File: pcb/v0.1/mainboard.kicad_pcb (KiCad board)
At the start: 2 copper layers, 123 parts, among them J1 Conn_01x02_Pin, J10 Conn_01x02_Pin, J11 Conn_01x02_Pin, J12 Conn_02x08_Odd_Even, J13 Conn_02x08_Odd_Even, J2 TYPE_C_Receptacle, J3 Conn_01x04_Pin, J4 TYPE_C_Receptacle, J5 TYPE_C_Receptacle, J6 22s_disp_connector, J7 ComputeModule5-CM5_connector, J8 Micro_SD_molex, J9 AudioJack3, Q1 MMBT2222A, SW1 SW_Push_45deg, U1 AP2112K-3.3TRG1, U2 Nexperia PUSB3FR4Z, U3 Nexperia PUSB3FR4Z, U4 PCM5102A, U5 RT9742GGJ5, U6 RT9742GGJ5, U7 MDBT50Q-P1MV2, U8 AP22653W6-7, Y1 O_32.768kHz

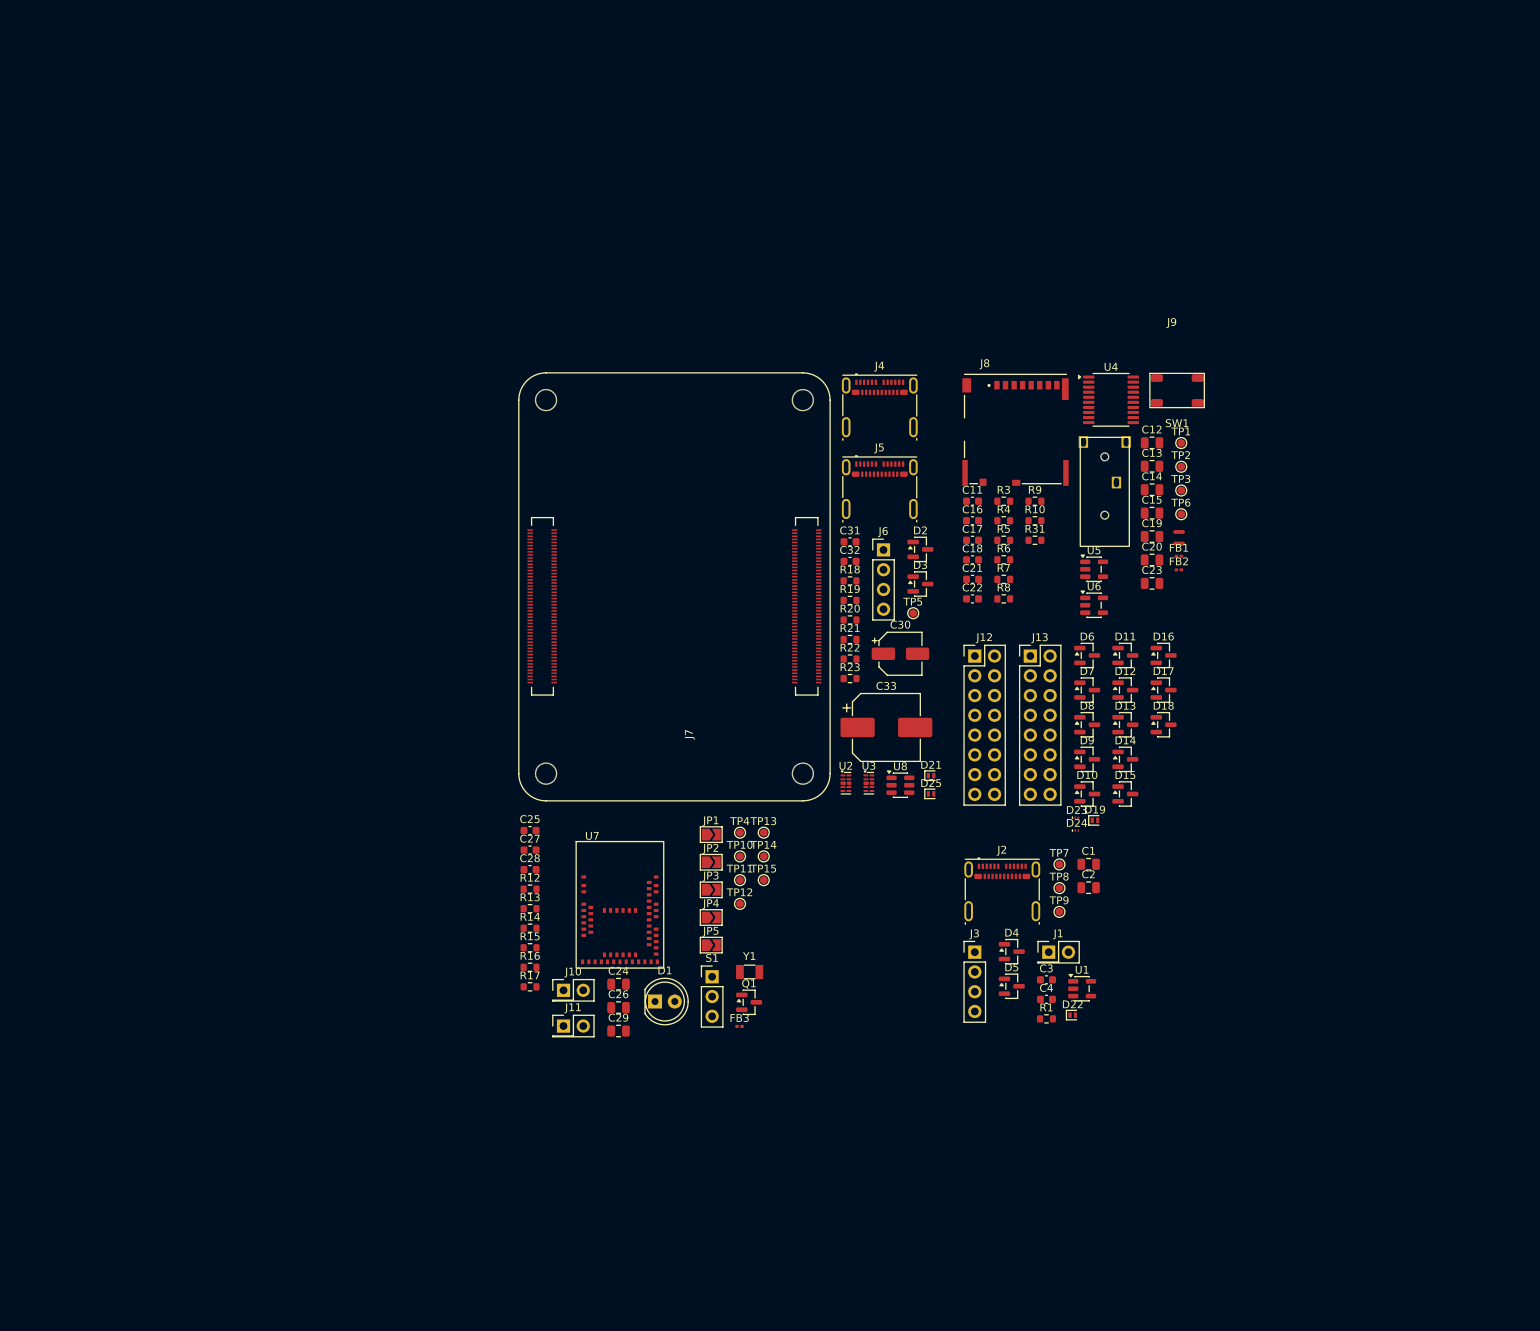
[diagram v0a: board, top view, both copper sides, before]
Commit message: Board setup and basic layout grouping
* Added board setup settings according to JLCpcbs manufacturing minimums
  (and generous extra)
* Grouped related components on the pcb
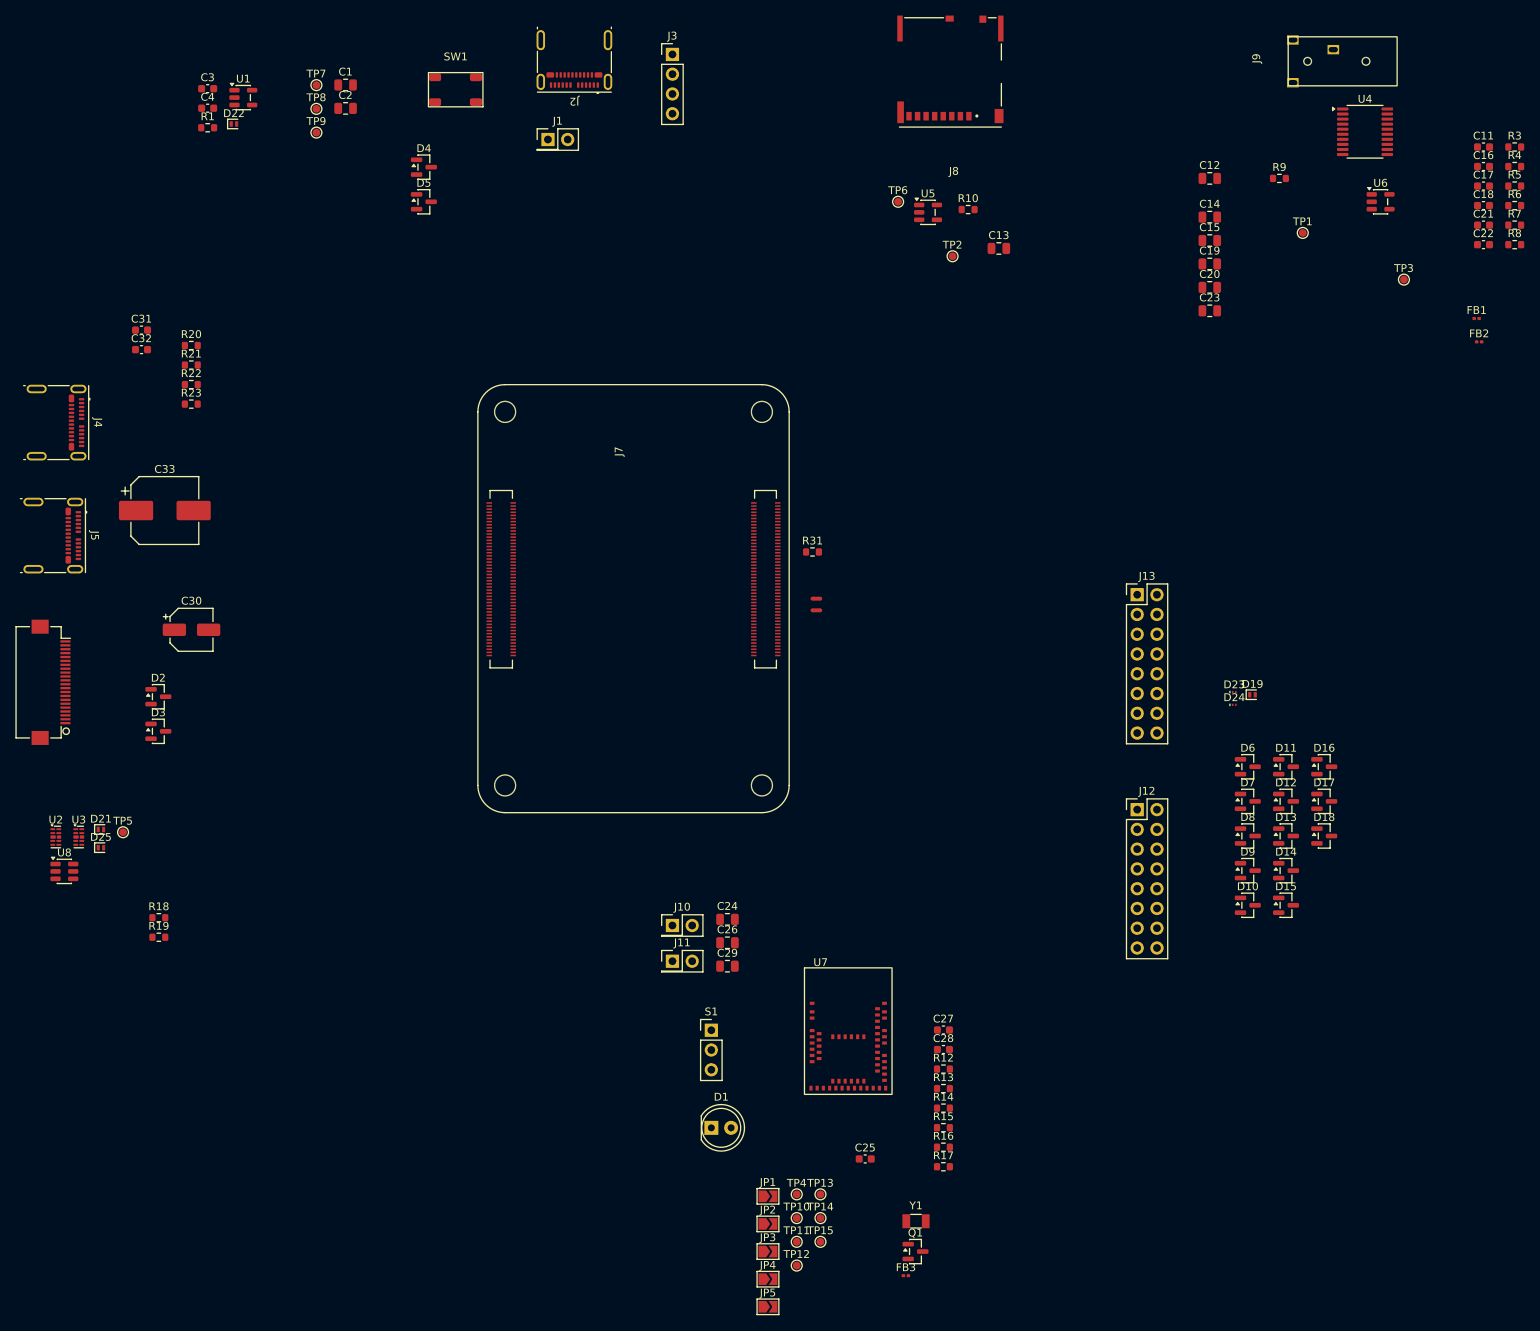
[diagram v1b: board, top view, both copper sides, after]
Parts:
- J6: footprint Connector_PinHeader_2.54mm:PinHeader_1x04_P2.54mm_Vertical -> CM5IO:Hirose_FH12-22S-0.5SH_1x22-1MP_P0.50mm_Horizontal
- moved R1 157.3 mm to (50.3, 54.5)
- moved U1 157.3 mm to (54.9, 50.6)
- moved C3 157.3 mm to (50.3, 49.5)
- moved C4 157.3 mm to (50.3, 52.0)
- moved D22 157.3 mm to (53.6, 54.0)
- moved C1 138.4 mm to (68.0, 49.0)
- moved C2 138.4 mm to (68.0, 52.0)
- moved TP7 138.4 mm to (64.2, 49.0)
- moved TP8 138.4 mm to (64.2, 52.1)
- moved TP9 138.4 mm to (64.2, 55.1)
- moved D5 126.0 mm to (78.1, 64.0)
- moved D4 126.0 mm to (78.1, 59.5)
- moved J1 122.7 mm to (94.0, 56.0)
- moved J3 121.7 mm to (110.0, 45.1)
- moved J2 120.1 mm to (97.4, 45.8), turned to 180 degrees
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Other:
- copper layers 2 -> 4
- rule pad_to_mask_clearance: 0 -> 0.1

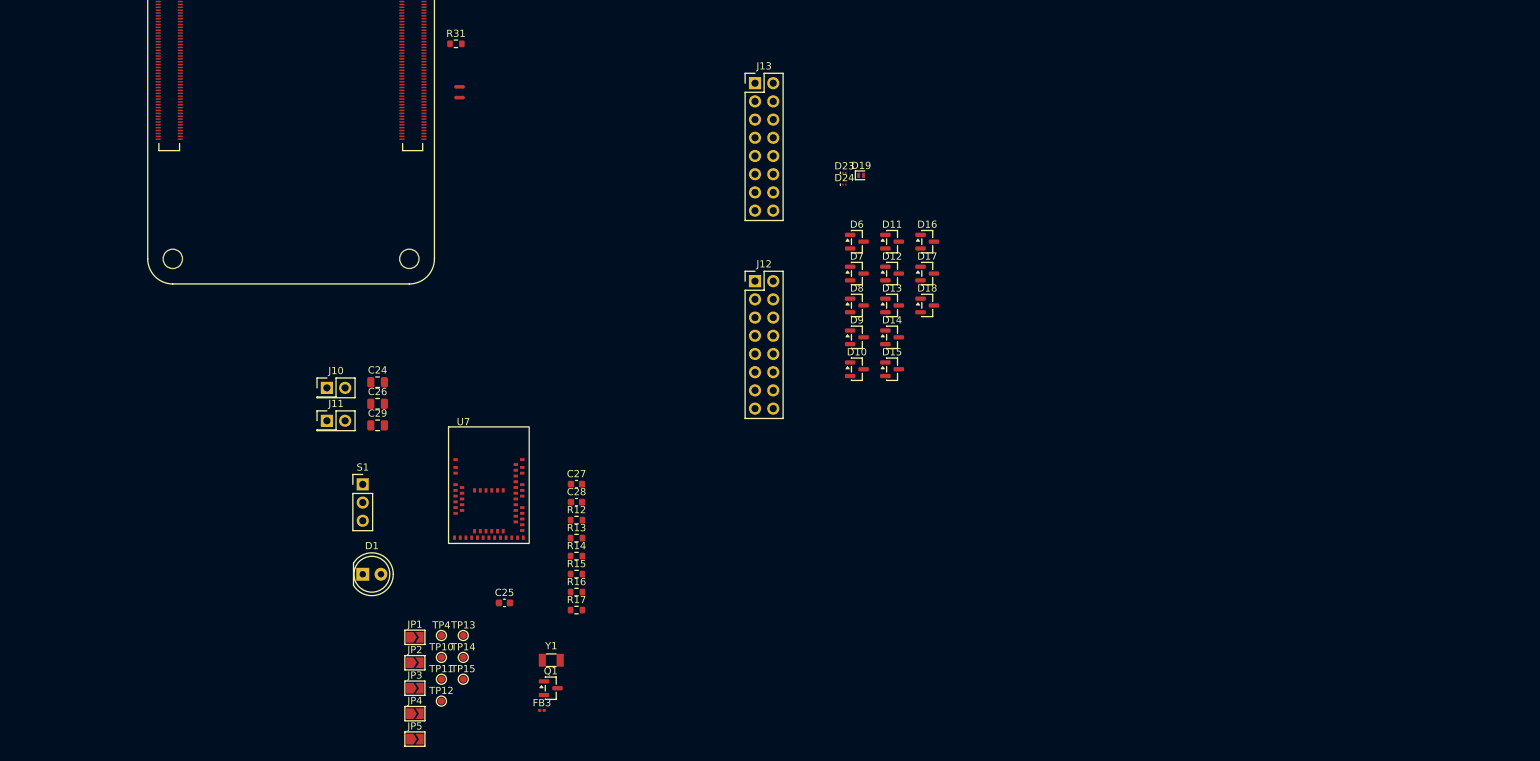
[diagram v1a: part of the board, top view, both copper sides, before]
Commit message: Rough layout of the co processor
First pass layout of where I think the components belonging to the co
processor will go. Most of it isn't wired up yet and wont be until
everything else has its place.
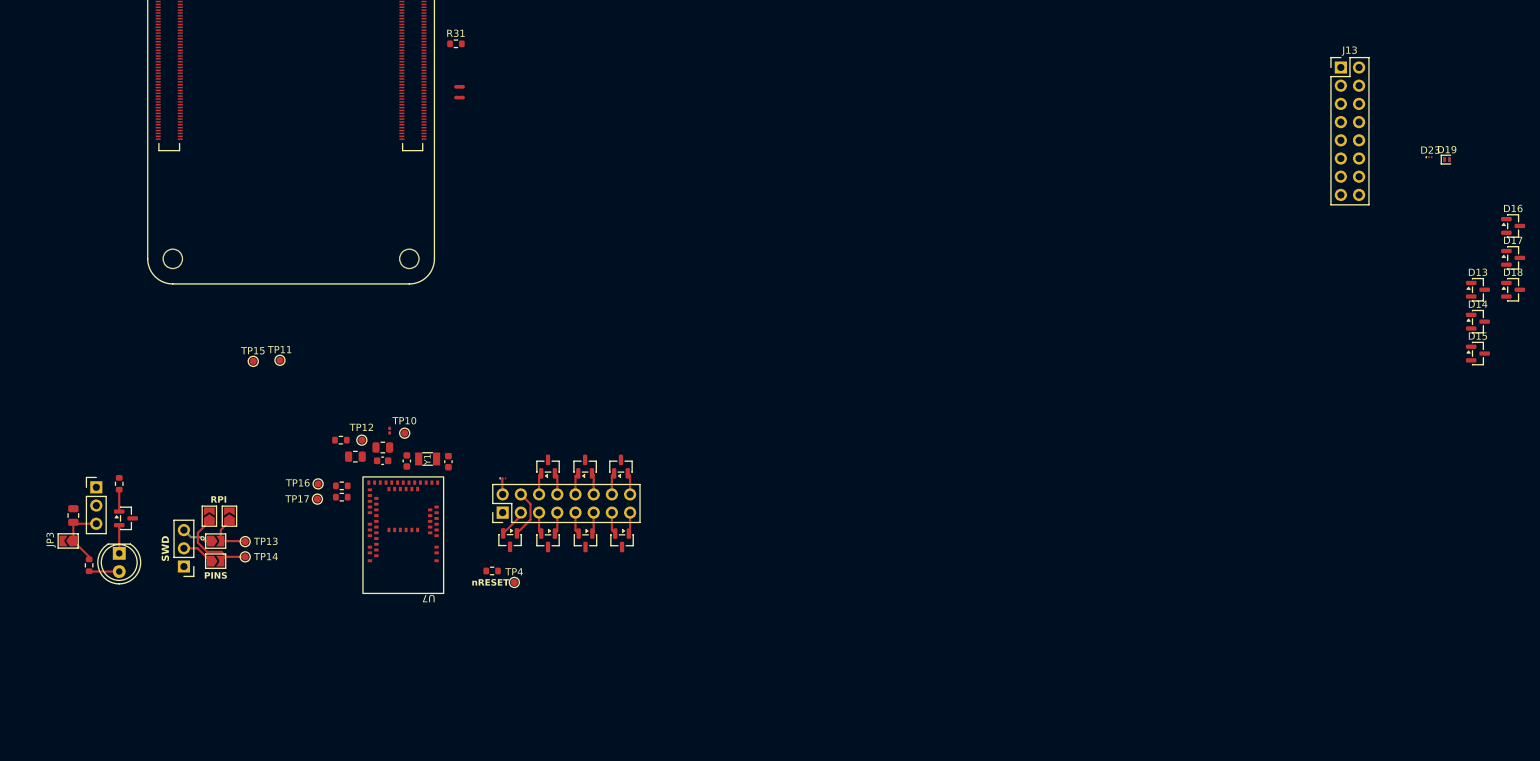
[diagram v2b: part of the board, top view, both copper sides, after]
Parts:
- removed J10: Conn_01x02_Pin, Connector_PinHeader_2.54mm:PinHeader_2x01_P2.54mm_Vertical
- added TP16: TestPoint, TestPoint:TestPoint_Pad_D1.0mm, F.Cu at (108.8, 170.4)
- added TP17: TestPoint, TestPoint:TestPoint_Pad_D1.0mm, F.Cu at (108.7, 172.5)
- J11: value Conn_01x02_Pin -> Conn_01x03_Pin; footprint Connector_PinHeader_2.54mm:PinHeader_2x01_P2.54mm_Vertical -> Connector_PinHeader_2.54mm:PinHeader_1x03_P2.54mm_Vertical
- moved D16 81.8 mm to (275.5, 134.4)
- moved D17 81.8 mm to (275.5, 138.9)
- moved D18 81.8 mm to (275.5, 143.3)
- moved D23 81.8 mm to (263.9, 124.8)
- moved J13 81.8 mm to (251.5, 112.3)
- moved D13 81.8 mm to (270.6, 143.3)
- moved D14 81.8 mm to (270.6, 147.8)
- moved D15 81.8 mm to (270.6, 152.2)
- moved D19 81.8 mm to (266.3, 125.2)
- moved R16 68.1 mm to (76.8, 181.8), turned to -90 degrees
- moved R17 66.2 mm to (81.0, 170.4), turned to -90 degrees
- moved D12 65.0 mm to (135.6, 178.2), turned to -90 degrees
- moved Q1 63.8 mm to (82.0, 175.2)
- moved D11 63.6 mm to (140.8, 178.3), turned to -90 degrees
- moved D24 62.7 mm to (134.7, 169.6)
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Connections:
- D10 pad 1: /Co processor/GP0.06 -> /Co processor/GP0.07
- D10 pad 2: /Co processor/GP0.07 -> /Co processor/GP0.06
- J11 pad 1: Net-(J11-Pin_1) -> GND
- J12 pad 1: /Co processor/GP0.15 -> GND
- J12 pad 10: /Co processor/GP0.06 -> /Co processor/GP0.20
- J12 pad 11: /Co processor/GP0.04/A2 -> /Co processor/GP0.13
- J12 pad 12: /Co processor/GP0.07 -> /Co processor/GP0.21
- J12 pad 13: /Co processor/GP0.05/A3 -> /Co processor/GP0.16
- J12 pad 14: /Co processor/GP0.08 -> /Co processor/GP0.19
- J12 pad 15: GND -> /Co processor/GP0.15
- J12 pad 16: /+3v3_LDO -> /Co processor/GP0.17
- J12 pad 2: /Co processor/GP0.17 -> /+3v3_LDO
- J12 pad 3: /Co processor/GP0.16 -> /Co processor/GP0.05/A3
- J12 pad 4: /Co processor/GP0.19 -> /Co processor/GP0.08
- J12 pad 5: /Co processor/GP0.13 -> /Co processor/GP0.04/A2
- J12 pad 6: /Co processor/GP0.21 -> /Co processor/GP0.07
- J12 pad 7: /Co processor/GP0.14 -> /Co processor/GP0.26
- J12 pad 8: /Co processor/GP0.20 -> /Co processor/GP0.06
- J12 pad 9: /Co processor/GP0.26 -> /Co processor/GP0.14
- JP1 pad 1: Net-(J11-Pin_1) -> Net-(J11-Pin_3)
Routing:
- net /Co processor/nSWDCLK: track 0.00 -> 12.1 mm
- net Net-(JP3-A): track 0.00 -> 9.37 mm
- net /Co processor/nSWDIO: track 0.00 -> 6.98 mm
- net /Co processor/GP0.08: track 0.00 -> 6.78 mm
- net Net-(J11-Pin_2): track 0.00 -> 4.44 mm
- net Net-(J11-Pin_3): track 0.00 -> 4.33 mm, vias 0 -> 1
- net Net-(D1-A): track 0.00 -> 4.22 mm
- net Net-(D1-K): track 0.00 -> 3.93 mm
- net /Co processor/GP0.05/A3: track 0.00 -> 3.92 mm
- net /Co processor/GP0.16: track 0.00 -> 3.12 mm
- net /Co processor/GP0.14: track 0.00 -> 3.11 mm
- net /Co processor/GP0.20: track 0.00 -> 3.10 mm
- net /Co processor/GP0.06: track 0.00 -> 3.08 mm
- net /Co processor/GP0.17: track 0.00 -> 3.07 mm
- net /Co processor/GP0.26: track 0.00 -> 3.07 mm
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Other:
- board text added: "PINS"
- board text added: "RPI"
- board text added: "SWD"
- board text added: "nRESET"

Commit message: Rough layout for power, SD and audio
Added the rough layout for the power input USB port, the 3v3 regulator,
the micro SD card and the entire audio subsystem including the dac and
its high side switch.
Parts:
- moved R8 91.3 mm to (134.0, 34.3), turned to 90 degrees
- moved C22 90.7 mm to (131.6, 31.9)
- moved R7 90.1 mm to (130.3, 47.0)
- moved R6 89.3 mm to (130.3, 48.6)
- moved R5 88.7 mm to (130.3, 50.2)
- moved C21 86.9 mm to (134.7, 31.9)
- moved R3 86.5 mm to (131.9, 51.9)
- moved C16 86.1 mm to (131.2, 36.8), turned to 180 degrees
- moved FB2 85.1 mm to (140.4, 38.6), turned to 180 degrees
- moved C18 83.7 mm to (135.3, 36.8)
- moved R4 83.5 mm to (135.1, 51.9)
- moved FB1 80.3 mm to (140.4, 45.4), turned to 180 degrees
- moved C11 80.3 mm to (134.3, 49.3)
- moved C17 78.6 mm to (138.4, 41.4), turned to -90 degrees
- moved TP3 67.3 mm to (143.1, 45.5)
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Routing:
- net /+5v: track 0.00 -> 38.2 mm, vias 0 -> 1
- net Net-(J1-Pin_2): track 0.00 -> 9.32 mm
- net /+3v3_LDO: track 2.25 -> 9.54 mm
- net /GPIO/CAPM: track 0.00 -> 5.14 mm
- net /GPIO/CAPP: track 0.00 -> 3.24 mm
- net GND: track 0.00 -> 3.16 mm, vias 0 -> 2
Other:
- board text added: "Can make a silkscreen box around each group of components"
- board text added: "GND"
- board text added: "VBUS"
- board text added: "comment"

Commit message: Initial rough layout and edge.cuts
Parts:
- moved D15 168.8 mm to (142.7, 42.1)
- moved D14 162.7 mm to (142.7, 47.1)
- moved D18 160.7 mm to (153.0, 39.4), turned to 180 degrees
- moved D13 157.0 mm to (142.7, 52.3)
- moved D17 154.6 mm to (152.9, 44.6), turned to 180 degrees
- moved D19 149.6 mm to (148.4, 33.1)
- moved D16 149.0 mm to (152.9, 49.8), turned to 180 degrees
- moved D23 147.7 mm to (144.0, 38.6), turned to -90 degrees
- moved D7 143.0 mm to (174.3, 37.1), turned to 0 degrees
- moved D6 138.9 mm to (174.3, 42.2), turned to 0 degrees
- moved D11 135.0 mm to (174.3, 47.5), turned to 0 degrees
- moved TP4 132.0 mm to (173.6, 57.6), turned to 90 degrees
- moved D9 131.3 mm to (164.0, 37.3), turned to 180 degrees
- moved D12 131.3 mm to (174.3, 52.8), turned to 0 degrees
- moved R15 127.9 mm to (172.0, 60.7), turned to -90 degrees
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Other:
- board outline added: 156.4 x 94.8 mm

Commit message: Calculated USB diff pair impedance stuff
I am specifically committing this so it cannot get lost through any
bugs. Nothing has actually changed on the PCB other than board setup and
net classes.
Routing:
- net /HighSpeed/USB3-0-TX_N: track 0.00 -> 2.51 mm
- net /HighSpeed/USB3-0-TX_P: track 0.00 -> 2.18 mm
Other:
- board text added: "Note: Diff impedences calculated for JLCPCB 3313 stackup"
